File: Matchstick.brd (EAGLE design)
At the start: 72 x 24 mm, 26 parts, among them IC1 74HCT125D, J1 M5STICK_PINOUT, J2 JST-SH 4 Position Connector, J3 USB_A_PTH_MALE, U1 M5STAMP PICO

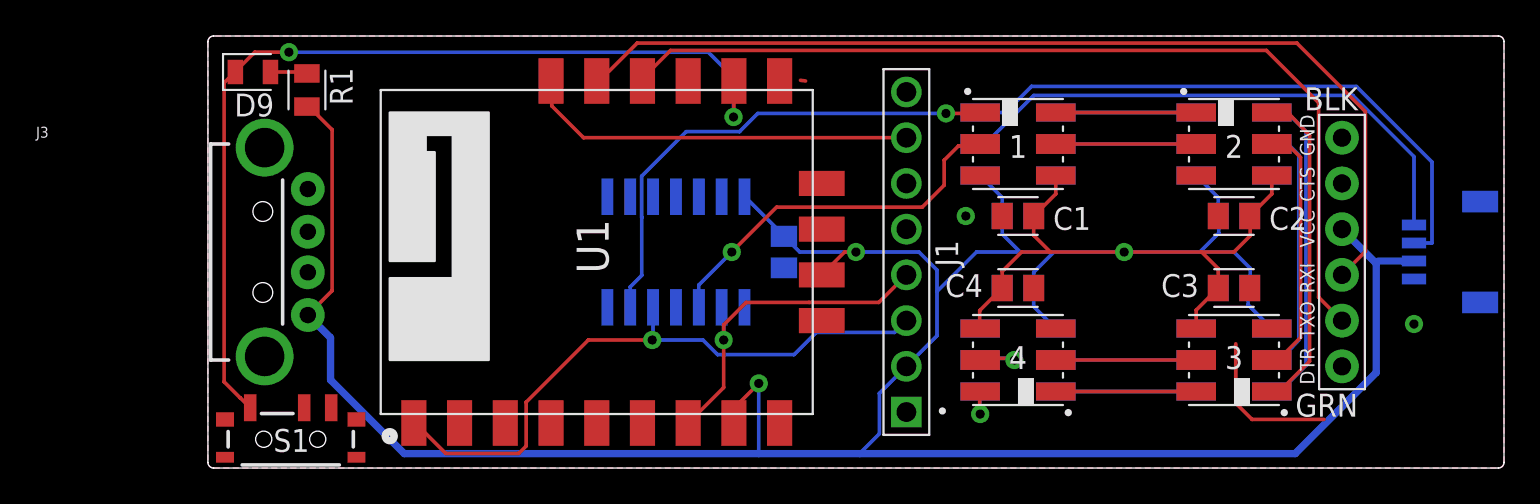
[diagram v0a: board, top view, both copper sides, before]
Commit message: Fixing RX/TX cross-wire
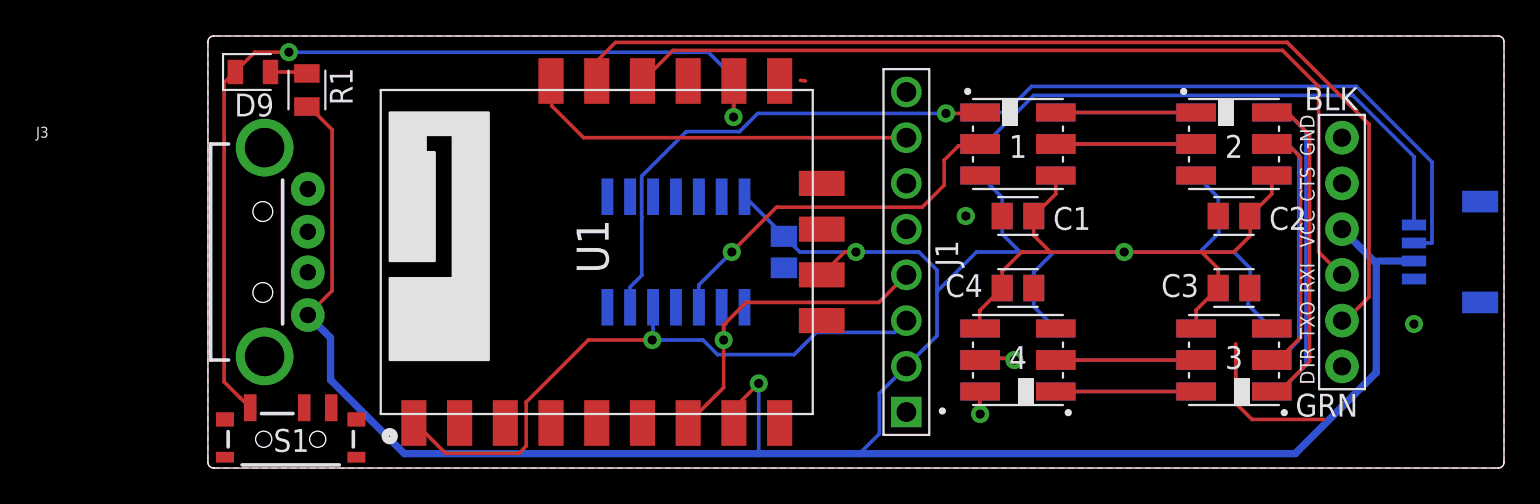
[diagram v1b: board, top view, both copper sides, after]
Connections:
- removed net G1: J4.P$3, U1.18
- removed net G3: J4.P$2, U1.17
- new net RX: J4.P$3, U1.17
- new net TX: J4.P$2, U1.18
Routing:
- net TX: track 0.00 -> 58.0 mm
- net G1: track 54.8 -> 0.00 mm
- net G3: track 52.2 -> 0.00 mm
- net RX: track 0.00 -> 50.1 mm
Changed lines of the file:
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@@
 <layer number="14" name="Route14" color="22" fill="1" visible="no" active="no"/>
 <layer number="15" name="Route15" color="23" fill="1" visible="no" active="no"/>
-<layer number="16" name="Bottom" color="1" fill="1" visible="yes" active="yes"/>
+<layer number="16" name="Bottom" color="1" fill="1" visible="no" active="yes"/>
 <layer number="17" name="Pads" color="2" fill="1" visible="yes" active="yes"/>
 <layer number="18" name="Vias" color="2" fill="1" visible="yes" active="yes"/>
@@
 <layer number="20" name="Dimension" color="24" fill="1" visible="yes" active="yes"/>
 <layer number="21" name="tPlace" color="7" fill="1" visible="yes" active="yes"/>
-<layer number="22" name="bPlace" color="7" fill="1" visible="yes" active="yes"/>
+<layer number="22" name="bPlace" color="7" fill="1" visible="no" active="yes"/>
 <layer number="23" name="tOrigins" color="15" fill="1" visible="yes" active="yes"/>
-<layer number="24" name="bOrigins" color="15" fill="1" visible="yes" active="yes"/>
+<layer number="24" name="bOrigins" color="15" fill="1" visible="no" active="yes"/>
 <layer number="25" name="tNames" color="7" fill="1" visible="yes" active="yes"/>
-<layer number="26" name="bNames" color="7" fill="1" visible="yes" active="yes"/>
+<layer number="26" name="bNames" color="7" fill="1" visible="no" active="yes"/>
 <layer number="27" name="tValues" color="7" fill="1" visible="no" active="yes"/>
 <layer number="28" name="bValues" color="7" fill="1" visible="no" active="yes"/>
@@
 <layer number="38" name="bTest" color="7" fill="1" visible="no" active="yes"/>
 <layer number="39" name="tKeepout" color="4" fill="11" visible="yes" active="yes"/>
-<layer number="40" name="bKeepout" color="1" fill="11" visible="yes" active="yes"/>
+<layer number="40" name="bKeepout" color="1" fill="11" visible="no" active="yes"/>
 <layer number="41" name="tRestrict" color="4" fill="10" visible="yes" active="yes"/>
-<layer number="42" name="bRestrict" color="1" fill="10" visible="yes" active="yes"/>
+<layer number="42" name="bRestrict" color="1" fill="10" visible="no" active="yes"/>
 <layer number="43" name="vRestrict" color="2" fill="10" visible="no" active="yes"/>
 <layer number="44" name="Drills" color="7" fill="1" visible="no" active="yes"/>
@@
 <layer number="50" name="dxf" color="7" fill="1" visible="no" active="no"/>
 <layer number="51" name="tDocu" color="7" fill="1" visible="yes" active="yes"/>
-<layer number="52" name="bDocu" color="7" fill="1" visible="yes" active="yes"/>
+<layer number="52" name="bDocu" color="7" fill="1" visible="no" active="yes"/>
 <layer number="53" name="tGND_GNDA" color="7" fill="9" visible="no" active="no"/>
 <layer number="54" name="bGND_GNDA" color="1" fill="9" visible="no" active="no"/>
@@
 <wire x1="1.8052" y1="3.8948" x2="2.35" y2="3.35" width="0.2032" layer="1"/>
 </signal>
-<signal name="G1">
-<contactref element="U1" pad="18"/>
-<wire x1="21.6" y1="21.5" x2="21.73895" y2="21.5" width="0.2032" layer="1"/>
-<wire x1="21.73895" y1="21.5" x2="23.84535" y2="23.6064" width="0.2032" layer="1"/>
-<wire x1="23.84535" y1="23.6064" x2="60.4936" y2="23.6064" width="0.2032" layer="1"/>
-<wire x1="60.4936" y1="23.6064" x2="64.3" y2="19.8" width="0.2032" layer="1"/>
-<contactref element="J4" pad="P$3"/>
-<wire x1="64.3" y1="19.8" x2="64.3" y2="12.03" width="0.2032" layer="1"/>
-<wire x1="64.3" y1="12.03" x2="63" y2="10.73" width="0.2032" layer="1"/>
-</signal>
-<signal name="G3">
-<contactref element="U1" pad="17"/>
-<wire x1="24.14" y1="21.5" x2="24.14" y2="21.64" width="0.2032" layer="1"/>
-<wire x1="24.14" y1="21.64" x2="25.7" y2="23.2" width="0.2032" layer="1"/>
-<wire x1="25.7" y1="23.2" x2="58.8" y2="23.2" width="0.2032" layer="1"/>
-<wire x1="58.8" y1="23.2" x2="61.7" y2="20.3" width="0.2032" layer="1"/>
-<contactref element="J4" pad="P$2"/>
-<wire x1="63" y1="8.19" x2="61.7" y2="9.49" width="0.2032" layer="1"/>
-<wire x1="61.7" y1="9.49" x2="61.7" y2="20.3" width="0.2032" layer="1"/>
-</signal>
 <signal name="CI$5">
 <contactref element="4" pad="P5"/>
@@
 <wire x1="5.4195" y1="22" x2="5.5" y2="21.9195" width="0.2032" layer="1"/>
 </signal>
+<signal name="RX">
+<contactref element="U1" pad="17"/>
+<contactref element="J4" pad="P$3"/>
+<wire x1="24.14" y1="21.5" x2="25.84" y2="23.2" width="0.2032" layer="1"/>
+<wire x1="59.7" y1="23.2" x2="61.7" y2="21.2" width="0.2032" layer="1"/>
+<wire x1="61.7" y1="21.2" x2="61.7" y2="12" width="0.2032" layer="1"/>
+<wire x1="61.7" y1="12" x2="62.97" y2="10.73" width="0.2032" layer="1"/>
+<wire x1="62.97" y1="10.73" x2="63" y2="10.73" width="0.2032" layer="1"/>
+<wire x1="25.84" y1="23.2" x2="59.7" y2="23.2" width="0.2032" layer="1"/>
+</signal>
+<signal name="TX">
+<contactref element="J4" pad="P$2"/>
+<contactref element="U1" pad="18"/>
+<wire x1="21.6" y1="21.5" x2="21.6" y2="22.6" width="0.2032" layer="1"/>
+<wire x1="21.6" y1="22.6" x2="22.6444" y2="23.6444" width="0.2032" layer="1"/>
+<wire x1="22.6444" y1="23.6444" x2="59.9556" y2="23.6444" width="0.2032" layer="1"/>
+<wire x1="64.5" y1="19.1" x2="64.5" y2="9.5" width="0.2032" layer="1"/>
+<wire x1="64.5" y1="9.5" x2="63.19" y2="8.19" width="0.2032" layer="1"/>
+<wire x1="63.19" y1="8.19" x2="63" y2="8.19" width="0.2032" layer="1"/>
+<wire x1="59.9556" y1="23.6444" x2="64.5" y2="19.1" width="0.2032" layer="1"/>
+</signal>
 </signals>
